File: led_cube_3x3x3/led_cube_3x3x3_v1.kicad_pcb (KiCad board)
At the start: 2 copper layers, 2 parts, among them IC1 ATMEGA8A-P

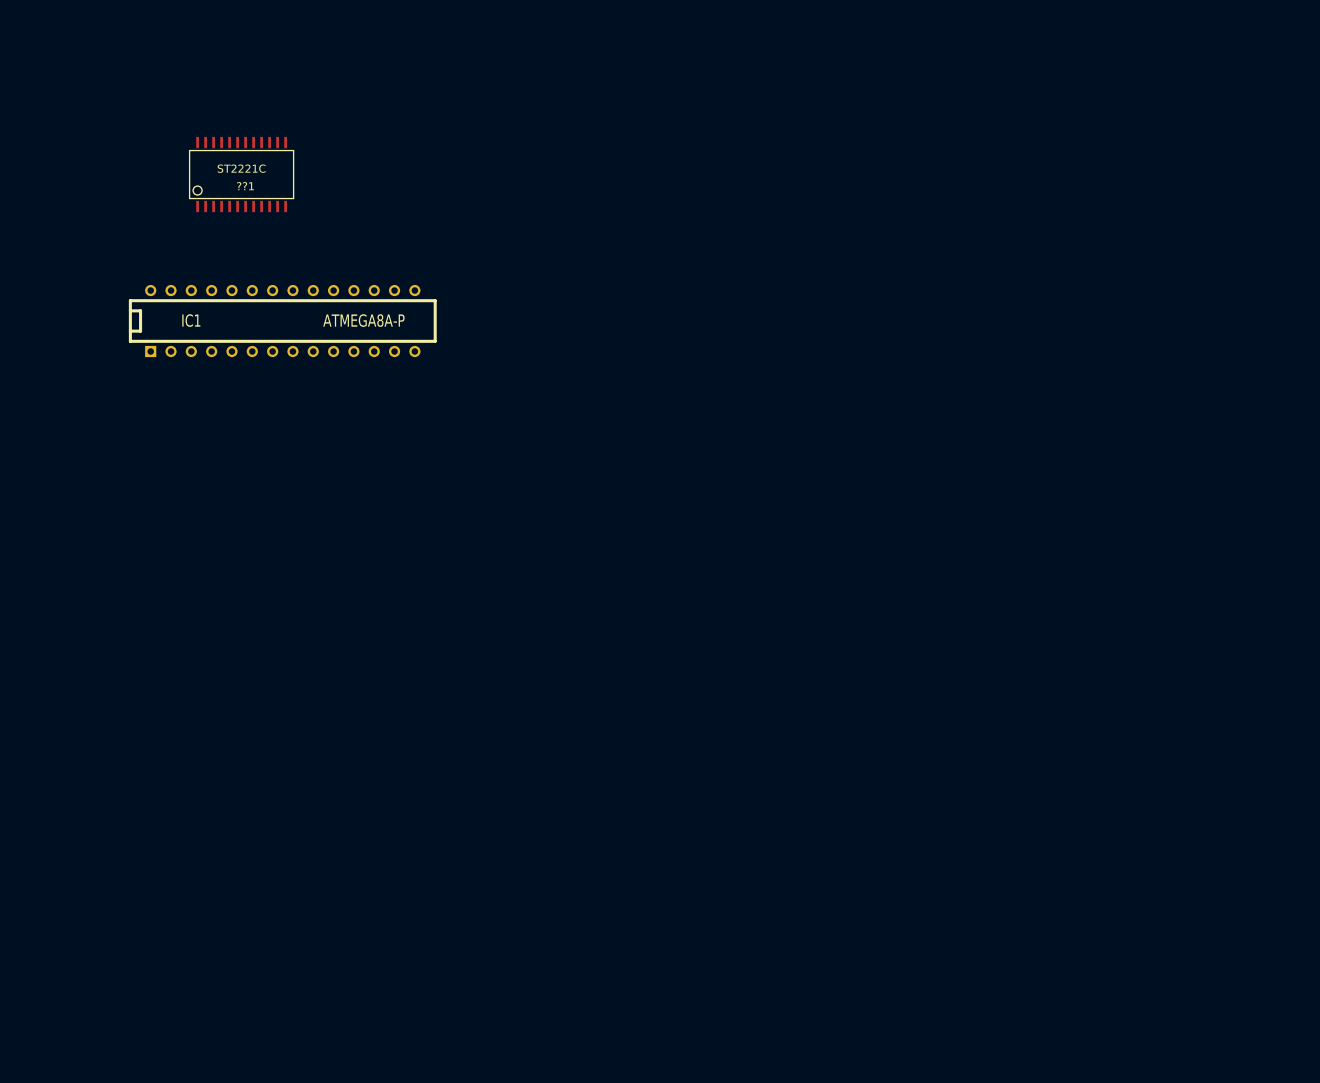
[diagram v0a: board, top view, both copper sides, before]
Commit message: led cube sch v1
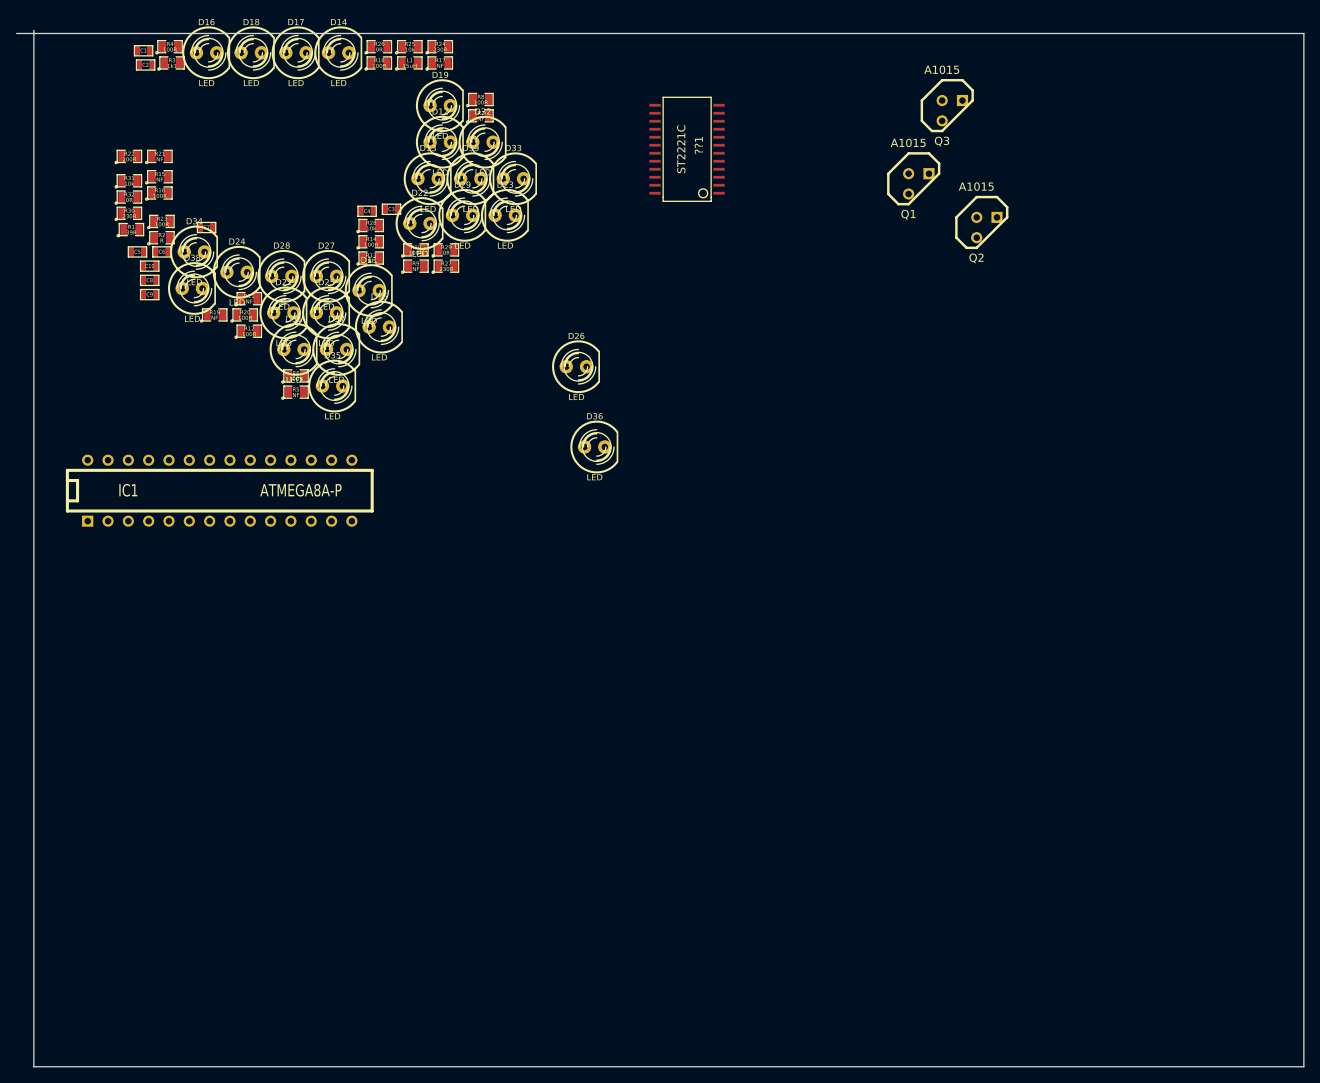
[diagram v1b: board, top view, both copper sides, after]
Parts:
- added C1: 100n, SM0603, F.Cu at (31.8, 17.5)
- added C10: C, SM0603, F.Cu at (32.5, 44.5)
- added C2: 100n, SM0603, F.Cu at (32.0, 19.3)
- added C3: C, SM0603, F.Cu at (62.7, 37.3)
- added C4: C, SM0603, F.Cu at (59.7, 37.6)
- added C5: C, SM0603, F.Cu at (31.0, 42.7)
- added C6: C, SM0603, F.Cu at (34.0, 42.7)
- added C7: C, SM0603, F.Cu at (39.6, 39.6)
- added C8: C, SM0603, F.Cu at (32.5, 46.2)
- added C9: C, SM0603, F.Cu at (32.5, 48.0)
- added D11: LED, LED-5MM, F.Cu at (59.9, 47.5)
- added D12: LED, LED-5MM, F.Cu at (68.8, 29.0)
- added D13: LED, LED-5MM, F.Cu at (67.3, 33.5)
- added D14: LED, LED-5MM, F.Cu at (56.1, 17.8)
- added D15: LED, LED-5MM, F.Cu at (61.2, 52.1)
- added D16: LED, LED-5MM, F.Cu at (39.6, 17.8)
- added D17: LED, LED-5MM, F.Cu at (50.8, 17.8)
- added D18: LED, LED-5MM, F.Cu at (45.2, 17.8)
- added D19: LED, LED-5MM, F.Cu at (68.8, 24.4)
- added D21: LED, LED-5MM, F.Cu at (49.3, 50.3)
- added D22: LED, LED-5MM, F.Cu at (66.3, 39.1)
- added D23: LED, LED-5MM, F.Cu at (77.0, 38.1)
- added D24: LED, LED-5MM, F.Cu at (43.4, 45.2)
- added D25: LED, LED-5MM, F.Cu at (54.6, 50.3)
- added D26: LED, LED-5MM, F.Cu at (85.9, 57.0)
- added D27: LED, LED-5MM, F.Cu at (54.6, 45.7)
- added D28: LED, LED-5MM, F.Cu at (49.0, 45.7)
- added D29: LED, LED-5MM, F.Cu at (71.6, 38.1)
- added D31: LED, LED-5MM, F.Cu at (50.5, 54.9)
- added D32: LED, LED-5MM, F.Cu at (74.2, 29.0)
- added D33: LED, LED-5MM, F.Cu at (78.0, 33.5)
- added D34: LED, LED-5MM, F.Cu at (38.1, 42.7)
- added D35: LED, LED-5MM, F.Cu at (55.4, 59.4)
- added D36: LED, LED-5MM, F.Cu at (88.1, 67.1)
- added D37: LED, LED-5MM, F.Cu at (55.9, 54.9)
- added D38: LED, LED-5MM, F.Cu at (37.8, 47.2)
- added D39: LED, LED-5MM, F.Cu at (72.6, 33.5)
- added L1: 15uH, SM0805, F.Cu at (65.0, 19.1)
- added Q1: A1015, TO92, F.Cu at (128.7, 34.2)
- added Q2: A1015, TO92, F.Cu at (137.2, 39.6)
- added Q3: A1015, TO92, F.Cu at (132.8, 25.0)
- added R1: 39R, SM0805, F.Cu at (30.2, 39.9)
- added R10: 100R, SM0805, F.Cu at (65.8, 42.4)
- added R11: NF, SM0805, F.Cu at (45.0, 48.5)
- added R12: 100R, SM0805, F.Cu at (45.0, 52.6)
- added R13: NF, SM0805, F.Cu at (60.2, 43.4)
- added R14: 100R, SM0805, F.Cu at (60.2, 41.4)
- added R15: NF, SM0805, F.Cu at (33.8, 33.3)
- added R16: 100R, SM0805, F.Cu at (33.8, 35.3)
- added R17: NF, SM0805, F.Cu at (68.8, 19.1)
- added R18: 100R, SM0805, F.Cu at (61.2, 19.1)
- added R19: NF, SM0805, F.Cu at (40.6, 50.5)
- added R2: R, SM0805, F.Cu at (34.0, 40.9)
- added R20: 100R, SM0805, F.Cu at (44.5, 50.5)
- added R21: NF, SM0805, F.Cu at (33.8, 30.7)
- added R22: 100R, SM0805, F.Cu at (30.0, 30.7)
- added R23: 100R, SM0805, F.Cu at (34.0, 38.9)
- added R24: 230R, SM0805, F.Cu at (68.8, 17.0)
- added R25: 10k, SM0805, F.Cu at (65.0, 17.0)
- added R26: 0R, SM0805, F.Cu at (61.2, 17.0)
- added R27: 230R, SM0805, F.Cu at (69.6, 44.5)
- added R28: 10k, SM0805, F.Cu at (60.2, 39.4)
- added R29: 0R, SM0805, F.Cu at (69.6, 42.4)
- added R3: 1k1, SM0805, F.Cu at (35.3, 19.1)
- added R30: 230R, SM0805, F.Cu at (30.0, 37.8)
- added R31: 10k, SM0805, F.Cu at (30.0, 33.8)
- added R32: 0R, SM0805, F.Cu at (30.0, 35.8)
- added R4: 100R, SM0805, F.Cu at (35.1, 17.0)
- added R5: NF, SM0805, F.Cu at (50.8, 60.2)
- added R6: 100R, SM0805, F.Cu at (50.8, 58.2)
- added R7: NF, SM0805, F.Cu at (73.9, 25.7)
- added R8: 100R, SM0805, F.Cu at (73.9, 23.6)
- added R9: NF, SM0805, F.Cu at (65.8, 44.5)
- moved ??1 55.8 mm to (99.7, 29.8), turned to 90 degrees
- moved IC1 22.6 mm to (41.3, 72.5)
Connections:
- ??1 pad 1: (no net) -> GND
- ??1 pad 10: N-000003 -> Vert_6
- ??1 pad 11: N-000001 -> Vert_7
- ??1 pad 12: N-000004 -> Vert_8
- ??1 pad 13: N-000005 -> Vert_9
- ??1 pad 23: (no net) -> N-0000030
- ??1 pad 24: (no net) -> N-0000014
- ??1 pad 5: N-000006 -> Vert_1
- ??1 pad 6: N-0000051 -> Vert_2
- ??1 pad 7: N-0000054 -> Vert_3
- ??1 pad 8: N-0000048 -> Vert_4
- ??1 pad 9: N-000002 -> Vert_5
- IC1 pad 1: (no net) -> N-0000015
- IC1 pad 10: (no net) -> N-0000011
- IC1 pad 20: (no net) -> N-0000021
- IC1 pad 21: (no net) -> N-0000013
- IC1 pad 22: (no net) -> GND
- IC1 pad 7: (no net) -> N-0000015
- IC1 pad 8: (no net) -> GND
- IC1 pad 9: (no net) -> N-0000012
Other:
- board outline added: 160.9 x 129.5 mm

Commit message: led cube pcb v0.1
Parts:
- removed ??1: ST2221C, SSOP24-1
- removed D11, D12, D13, D14, D15, D16, D17, D18, D19, D21, D22, D23, D24, D25, D26, D27, D28, D29, D31, D32, D33, D34, D35, D36, D37, D38, D39: LED, LED-5MM
- added C11: 33p, SM0805, B.Cu at (260.1, 41.1)
- added C12: 100n, SM0603, B.Cu at (274.8, 74.2)
- added C13: 100n, SM0603, F.Cu at (289.0, 105.0)
- added C14: 10u, c_elec_6.3x5.3, F.Cu at (287.8, 92.5)
- added D1: LED_CUBE_3X3X3, LED_CUBE_3x3x3_22mm, F.Cu at (258.0, 76.0)
- added J1: Supply, con-ptr500+-AK500/2, B.Cu at (291.6, 31.2)
- added J2: ISP, pin_array_3x2, B.Cu at (277.9, 36.6)
- added J4: UART, PIN_ARRAY_3X1, B.Cu at (255.5, 59.7)
- added Q4: SFH320, PIN_ARRAY_2X1, B.Cu at (276.1, 59.7)
- added R33: 100R, SM0603, F.Cu at (276.5, 124.5)
- added R34: 2k, SM0603, B.Cu at (273.8, 56.4)
- added R35: 0R, SM0805, B.Cu at (289.1, 37.6)
- added U1: ST2221C, SSOP24-1, F.Cu at (275.8, 93.0)
- added U2: 24C512, DIP-8__300_SMD, B.Cu at (267.7, 74.2)
- added X1: 16MHz, Q_49U3HMS, B.Cu at (256.0, 43.2)
- C1, IC1: moved to B.Cu
- C10: value C -> 33p; footprint SM0603 -> SM0805; moved to B.Cu
- C2: value 100n -> 10u; footprint SM0603 -> c_elec_6.3x5.3; moved to B.Cu
- C3, C5, C7, C8, C9: value C -> 100n; moved to B.Cu
- C4, C6: value C -> 10u; footprint SM0603 -> c_elec_6.3x5.3; moved to B.Cu
- L1: footprint SM0805 -> SM1206; moved to B.Cu
- Q1, Q2, Q3: footprint TO92 -> TO92-123; moved to B.Cu
- R1: value 39R -> 10k; footprint SM0805 -> SM0603; moved to B.Cu
- R10, R6, R8: value 100R -> 0R; footprint SM0805 -> SM0603; moved to B.Cu
- R11: value NF -> 10k; footprint SM0805 -> SM0603; moved to B.Cu
- R12, R14, R16, R18, R20, R22: value 100R -> NF; footprint SM0805 -> SM0603
- R13, R15, R17, R19, R21: value NF -> 100R; footprint SM0805 -> SM0603
- R2: value R -> 10k; footprint SM0805 -> SM0603; moved to B.Cu
- R23: footprint SM0805 -> SM0603
- R24: value 230R -> NF; footprint SM0805 -> SM0603
- R25: value 10k -> 100R; footprint SM0805 -> SM0603
- R26: value 0R -> NF; footprint SM0805 -> SM0603
- R27: value 230R -> 100R; footprint SM0805 -> SM0603
- R28: value 10k -> NF; footprint SM0805 -> SM0603
- R29, R32: value 0R -> 100R; footprint SM0805 -> SM0603
- R3: value 1k1 -> 10k; footprint SM0805 -> SM0603; moved to B.Cu
- R30: value 230R -> 20R; footprint SM0805 -> SM0603
- R31: value 10k -> 1k1; footprint SM0805 -> SM0603
- R4: value 100R -> 20R; footprint SM0805 -> SM0603; moved to B.Cu
- R5, R7, R9: value NF -> 230R; footprint SM0805 -> SM0603; moved to B.Cu
- moved R1 277.4 mm to (305.6, 73.4), turned to 90 degrees
- moved R2 272.6 mm to (305.6, 65.3), turned to 90 degrees
- moved C1 272.3 mm to (298.7, 71.1), turned to 90 degrees
- moved R3 272.0 mm to (305.6, 49.8), turned to 270 degrees
- moved C5 267.7 mm to (298.7, 46.7), turned to 270 degrees
- moved C2 266.2 mm to (293.9, 67.1)
- moved R30 265.5 mm to (285.5, 110.0), turned to 180 degrees
- moved R31 264.5 mm to (276.0, 131.0), turned to 90 degrees
- moved R32 262.7 mm to (276.0, 128.0), turned to 270 degrees
- moved C6 260.0 mm to (293.9, 50.3)
- moved R4 249.7 mm to (284.0, 36.3), turned to 270 degrees
- moved C8 244.1 mm to (276.6, 45.2), turned to 270 degrees
- moved R15 243.8 mm to (261.0, 121.7), turned to 180 degrees
- moved C9 242.1 mm to (274.6, 47.8), turned to 270 degrees
- moved C3 237.4 mm to (298.7, 63.0), turned to 90 degrees
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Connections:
- C1 pad 1: N-0000021 -> GNDPWR
- C1 pad 2: GND -> +5V
- C10 pad 1: GND -> N-0000012
- C10 pad 2: +5V -> GND
- C2 pad 1: N-0000013 -> +5V
- C2 pad 2: GND -> GNDPWR
- C3 pad 1: N-0000012 -> GNDPWR
- C3 pad 2: GND -> +5V
- C4 pad 1: N-0000011 -> +5V
- C4 pad 2: GND -> GNDPWR
- C5 pad 1: N-0000015 -> GNDPWR
- C5 pad 2: GND -> +5V
- C6 pad 1: GND -> +5V
- C6 pad 2: N-0000014 -> GNDPWR
- C7 pad 1: GND -> /uCVcc
- C7 pad 2: N-0000014 -> GND
- C8 pad 1: GND -> /AVcc
- C8 pad 2: +5V -> GND
- C9 pad 1: GND -> /ARef
- C9 pad 2: +5V -> GND
- IC1 pad 1: N-0000015 -> ISP RST
- IC1 pad 10: N-0000011 -> N-0000013
- IC1 pad 11: (no net) -> SDI
- IC1 pad 12: (no net) -> LA
- IC1 pad 13: (no net) -> OE
- IC1 pad 14: (no net) -> Lev_1
- IC1 pad 15: (no net) -> Lev_2
- IC1 pad 17: (no net) -> ISP MOSI
- IC1 pad 18: (no net) -> ISP MISO
- IC1 pad 19: (no net) -> ISP SCK
- IC1 pad 2: (no net) -> RxD
- IC1 pad 20: N-0000021 -> /AVcc
- IC1 pad 21: N-0000013 -> /ARef
- IC1 pad 23: (no net) -> Lev_3
- IC1 pad 25: (no net) -> LIGHT_SENS
- IC1 pad 27: (no net) -> SDA
- IC1 pad 28: (no net) -> SCL
- IC1 pad 3: (no net) -> TxD
- IC1 pad 4: (no net) -> WP
- IC1 pad 6: (no net) -> CLK
- IC1 pad 7: N-0000015 -> /uCVcc
- L1 pad 1: N-0000021 -> +5V
- L1 pad 2: +5V -> /AVcc
- Q1 pad 1: +5V -> /A1C
- Q1 pad 2: N-0000022 -> +5V
- Q1 pad 3: N-000001 -> N-0000018
- Q2 pad 1: +5V -> /A2C
- Q2 pad 2: N-0000023 -> +5V
- Q2 pad 3: N-0000028 -> N-0000017
- Q3 pad 1: +5V -> /A3C
- Q3 pad 2: N-0000024 -> +5V
- Q3 pad 3: N-0000027 -> N-000007
- R1 pad 1: +5V -> N-0000018
- R1 pad 2: N-0000015 -> +5V
- R10 pad 1: Vert_3 -> N-000007
- R11 pad 1: Vert_4 -> ISP RST
- R11 pad 2: N-000004 (its old number) -> /uCVcc
- R12 pad 1: Vert_4 -> Vert_1
- R12 pad 2: N-000004 (its old number) -> /C1
- R13 pad 1: Vert_5 -> Vert_1
- R13 pad 2: N-000006 -> /C1
- R14 pad 1: Vert_5 -> Vert_2
- R14 pad 2: N-000006 -> /C2
- R15 pad 1: Vert_6 -> Vert_2
- R15 pad 2: N-000003 (its old number) -> /C2
- R16 pad 1: Vert_6 -> Vert_3
- R16 pad 2: N-000003 (its old number) -> /C3
- R17 pad 1: Vert_7 -> Vert_3
- R17 pad 2: N-000005 (its old number) -> /C3
- R18 pad 1: Vert_7 -> Vert_4
- R18 pad 2: N-000005 (its old number) -> /C4
- R19 pad 1: Vert_8 -> Vert_4
- R19 pad 2: N-000002 -> /C4
- R2 pad 1: +5V -> N-0000017
- R2 pad 2: N-0000014 -> +5V
- R20 pad 1: Vert_8 -> Vert_5
- R20 pad 2: N-000002 -> /C5
- R21 pad 1: Vert_9 -> Vert_5
- R21 pad 2: N-0000010 -> /C5
- R22 pad 1: Vert_9 -> Vert_6
- R22 pad 2: N-0000010 -> /C6
- R23 pad 1: N-0000019 -> Vert_6
- R23 pad 2: N-0000030 -> /C6
- R24 pad 1: (no net) -> Vert_7
- R24 pad 2: N-0000025 -> /C7
- R25 pad 1: N-0000022 -> Vert_7
- R25 pad 2: +5V -> /C7
- R26 pad 1: N-0000022 -> Vert_8
- R26 pad 2: N-0000025 -> /C8
- R27 pad 1: (no net) -> Vert_8
- R27 pad 2: N-0000026 -> /C8
- R28 pad 1: N-0000023 -> Vert_9
- R28 pad 2: +5V -> /C9
- R29 pad 1: N-0000023 -> Vert_9
- R29 pad 2: N-0000026 -> /C9
- R3 pad 1: GND -> N-000007
- R3 pad 2: N-0000020 -> +5V
- R30 pad 1: (no net) -> +5V
- R30 pad 2: N-0000035 -> N-0000014
- R31 pad 1: N-0000024 -> GNDPWR
- R31 pad 2: +5V -> N-0000010
- R32 pad 1: N-0000024 -> N-0000011
- R32 pad 2: N-0000035 -> N-0000010
- R4 pad 1: N-0000019 -> +5V
- R4 pad 2: N-0000020 -> /uCVcc
- R5 pad 1: Vert_1 -> Lev_1
- R6 pad 1: Vert_1 -> N-0000018
- R7 pad 1: Vert_2 -> Lev_2
- R8 pad 1: Vert_2 -> N-0000017
- R9 pad 1: Vert_3 -> Lev_3
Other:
- board size 160.9 x 129.5 mm -> 54 x 54 mm
- net class Current added: clearance 0.3048, trace_width 1.5, via_dia 1, via_drill 0.8
- net class Default: clearance 0.254 -> 0.3048; trace_width 0.254 -> 0.3556; via_dia 0.889 -> 1; via_drill 0.635 -> 0.8
- net class Supply added: clearance 0.3048, trace_width 0.635, via_dia 1, via_drill 0.8
- rule trace_clearance: 0.254 -> 0.3048
- rule via_min_drill: 0.508 -> 0.6
- rule via_min_size: 0.889 -> 0.9

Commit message: led cube pcb v1.0
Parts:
- removed C4, C6: 10u, c_elec_6.3x5.3
- removed C5: 100n, SM0603
- added D2: 5v1, SM1206POL2, F.Cu at (293.1, 73.5)
- added P1: CONN_1, PINTST, F.Cu at (267.0, 41.5)
- added P2: CONN_1, PINTST, F.Cu at (261.0, 31.5)
- added P3: CONN_1, PINTST, F.Cu at (269.0, 32.0)
- added P4: CONN_1, PINTST, F.Cu at (277.4, 53.8)
- added P5: CONN_1, PINTST, F.Cu at (253.0, 48.6)
- added P6: CONN_1, PINTST, F.Cu at (253.0, 35.1)
- C3, C8, L1, Q1, Q2, Q3, Q4, R34, U2: moved to F.Cu
- R30: footprint SM0603 -> SM1206
- R35: footprint SM0805 -> SM1206
- R4: footprint SM0603 -> SM1206; moved to F.Cu
- moved R28 109.6 mm to (306.4, 33.7), turned to 90 degrees
- moved R29 107.1 mm to (304.4, 33.7), turned to 90 degrees
- moved R23 89.5 mm to (306.3, 54.8), turned to 270 degrees
- moved R22 86.7 mm to (304.3, 54.8), turned to 270 degrees
- moved R26 84.0 mm to (282.4, 31.0), turned to 90 degrees
- moved R27 82.0 mm to (284.5, 31.0), turned to 90 degrees
- moved R25 79.9 mm to (255.5, 32.5), turned to 270 degrees
- moved R24 77.4 mm to (253.5, 32.5), turned to 270 degrees
- moved R16 75.9 mm to (306.8, 76.4), turned to 270 degrees
- moved R17 74.4 mm to (304.8, 76.4), turned to 270 degrees
- moved R21 69.1 mm to (280.0, 51.0), turned to 270 degrees
- moved R20 66.6 mm to (278.5, 51.0), turned to 270 degrees
- moved R32 65.6 mm to (285.0, 63.0)
- moved R33 65.6 mm to (285.0, 59.4)
- moved R31 65.1 mm to (285.0, 66.5)
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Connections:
- C12 pad 1: +5V -> /uCVcc
- IC1 pad 11: SDI -> (no net)
- IC1 pad 12: LA -> (no net)
- IC1 pad 13: OE -> SDI
- IC1 pad 14: Lev_1 -> LA
- IC1 pad 15: Lev_2 -> OE
- IC1 pad 16: (no net) -> CLK
- IC1 pad 23: Lev_3 -> LIGHT_SENS
- IC1 pad 24: (no net) -> Lev_3
- IC1 pad 25: LIGHT_SENS -> Lev_2
- IC1 pad 26: (no net) -> Lev_1
- IC1 pad 6: CLK -> (no net)
- J1 pad 2: GND -> GNDPWR
- L1 pad 1: +5V -> /uCVcc
- Q1 pad 1: /A1C -> +5V
- Q1 pad 2: +5V -> /A1C
- Q2 pad 1: /A2C -> +5V
- Q2 pad 2: +5V -> /A2C
- Q3 pad 1: /A3C -> +5V
- Q3 pad 2: +5V -> /A3C
- R35 pad 1: GND -> GNDPWR
- R35 pad 2: GNDPWR -> GND
- U1 pad 10: Vert_6 -> Vert_7
- U1 pad 11: Vert_7 -> Vert_8
- U1 pad 12: Vert_8 -> Vert_5
- U1 pad 13: Vert_9 -> Vert_2
- U1 pad 5: Vert_1 -> Vert_6
- U1 pad 6: Vert_2 -> Vert_3
- U1 pad 7: Vert_3 -> Vert_9
- U1 pad 8: Vert_4 -> Vert_1
- U1 pad 9: Vert_5 -> Vert_4
- U2 pad 1: +5V -> /uCVcc
- U2 pad 2: +5V -> /uCVcc
- U2 pad 8: +5V -> /uCVcc
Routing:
- net +5V: track 0.00 -> 136.0 mm
- net Vert_1: track 0.00 -> 119.3 mm
- net GND: track 0.00 -> 115.0 mm, vias 0 -> 2
- net /uCVcc: track 0.00 -> 97.2 mm, vias 0 -> 1
- net Vert_4: track 0.00 -> 86.3 mm
- net GNDPWR: track 0.00 -> 72.5 mm
- net ISP MOSI: track 0.00 -> 71.4 mm
- net WP: track 0.00 -> 61.9 mm
- net ISP MISO: track 0.00 -> 61.5 mm
- net ISP SCK: track 0.00 -> 57.0 mm
- net Vert_7: track 0.00 -> 54.2 mm
- net Vert_3: track 0.00 -> 46.9 mm
- net Vert_2: track 0.00 -> 42.8 mm
- net LA: track 0.00 -> 42.1 mm, vias 0 -> 1
- net SDI: track 0.00 -> 42.0 mm, vias 0 -> 1
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- added copper zone on B.Cu, net GND
- added copper zone on F.Cu, net GND
- added copper zone on F.Cu, net GNDPWR
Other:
- board size 54 x 54 mm -> 64 x 64 mm
- board text added: "Led Cube 3x3x3"
- board text added: "mic 102016"

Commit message: led cube sch pcp v2.0
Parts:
- added PINTST: Val*, PINTST, F.Cu at (114.5, 118.0)
- added PINTST: Val*, PINTST, F.Cu at (121.5, 126.0)
- added PINTST: Val*, PINTST, F.Cu at (118.5, 100.0)
- added PINTST: Val*, PINTST, F.Cu at (123.0, 117.0)
- added PINTST: Val*, PINTST, F.Cu at (136.8, 84.0)
- added PINTST: Val*, PINTST, F.Cu at (113.5, 104.0)
- added PINTST: Val*, PINTST, F.Cu at (141.0, 110.5)
- moved P4 149.8 mm to (129.5, 77.5)
- moved P5 145.6 mm to (113.9, 91.5)
- moved P6 145.1 mm to (114.8, 79.2)
- moved P3 144.7 mm to (130.8, 74.8)
- moved C1 144.1 mm to (154.6, 114.9)
- moved C13 144.1 mm to (153.1, 91.3)
- moved C14 144.1 mm to (153.1, 95.8)
- moved C2 144.1 mm to (154.6, 110.1)
- moved C8 144.1 mm to (128.9, 89.2)
- moved J1 144.1 mm to (153.1, 121.7)
- moved L1 144.1 mm to (131.2, 89.2)
- moved R15 144.1 mm to (144.4, 116.2)
- moved R27 144.1 mm to (147.0, 74.0)
- moved R30 144.1 mm to (150.8, 111.3)
- moved R35 144.1 mm to (143.2, 124.8)
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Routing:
- added copper zone on B.Cu, net GNDPWR
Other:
- board text added: "+5V"
- board text added: "GND"
- board text added: "ISP"
- board text added: "UART"
